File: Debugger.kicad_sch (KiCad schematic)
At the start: 24 parts, among them J1 Internal clock, J2 I/O, J3 NAND0, J4 NAND1, Q1 BC546, SW1 Single step, U1 NE555P, U2 74LS132, U3 74LS74

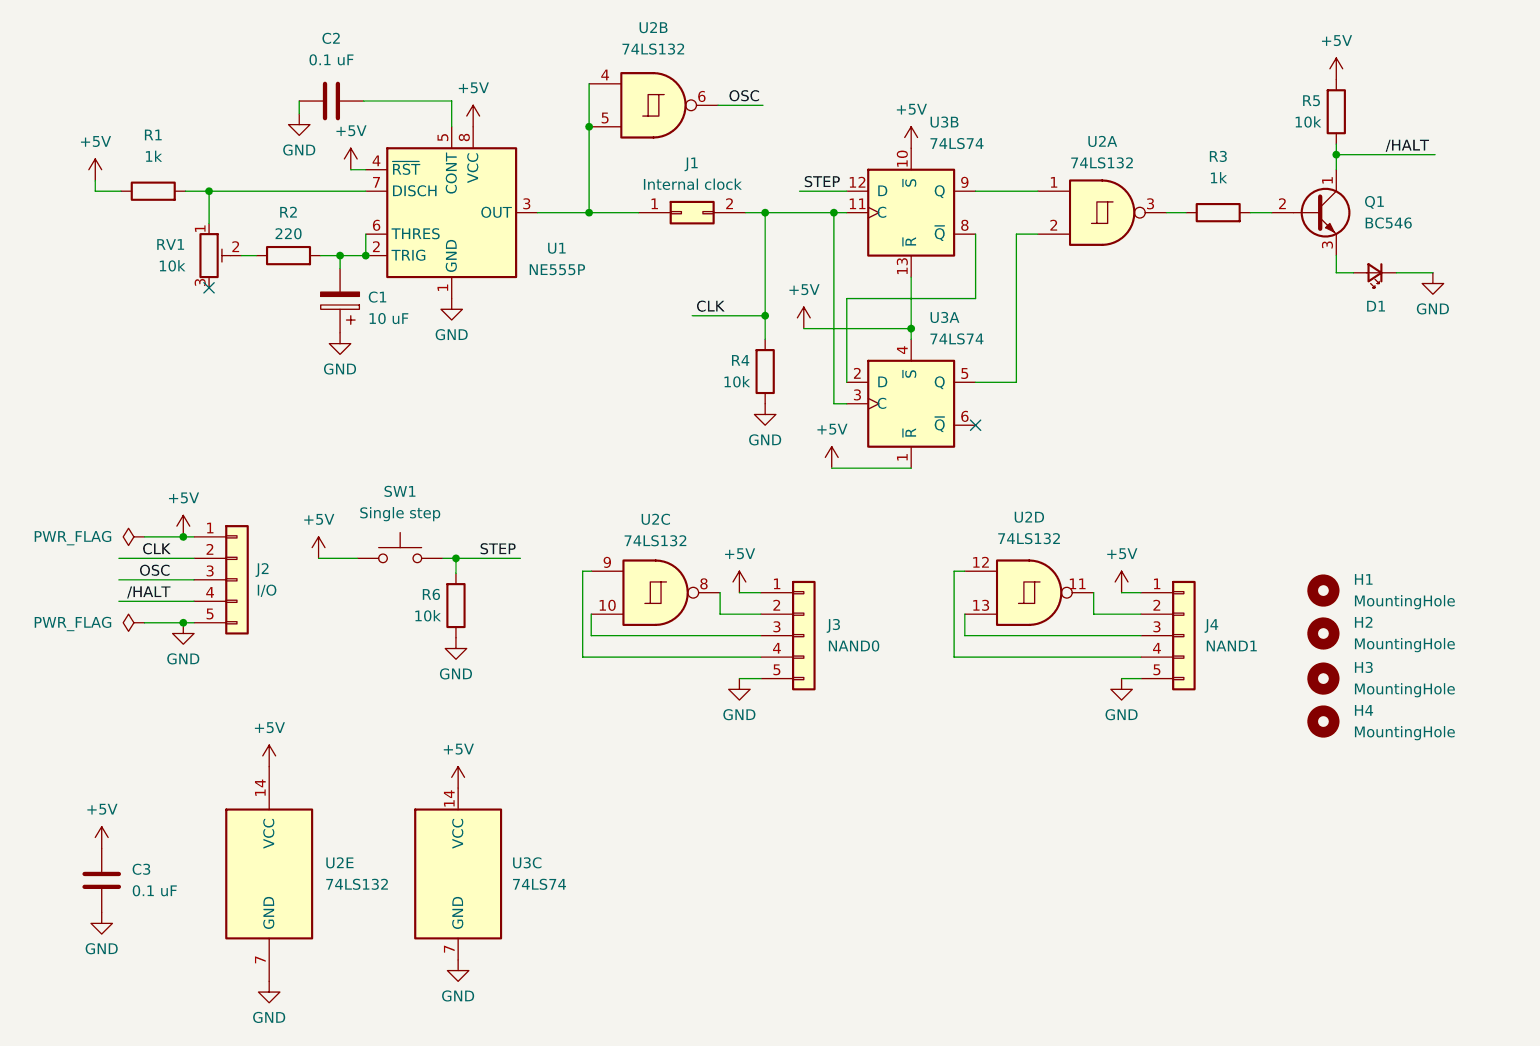
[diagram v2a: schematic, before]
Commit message: Board: add PCB drawing
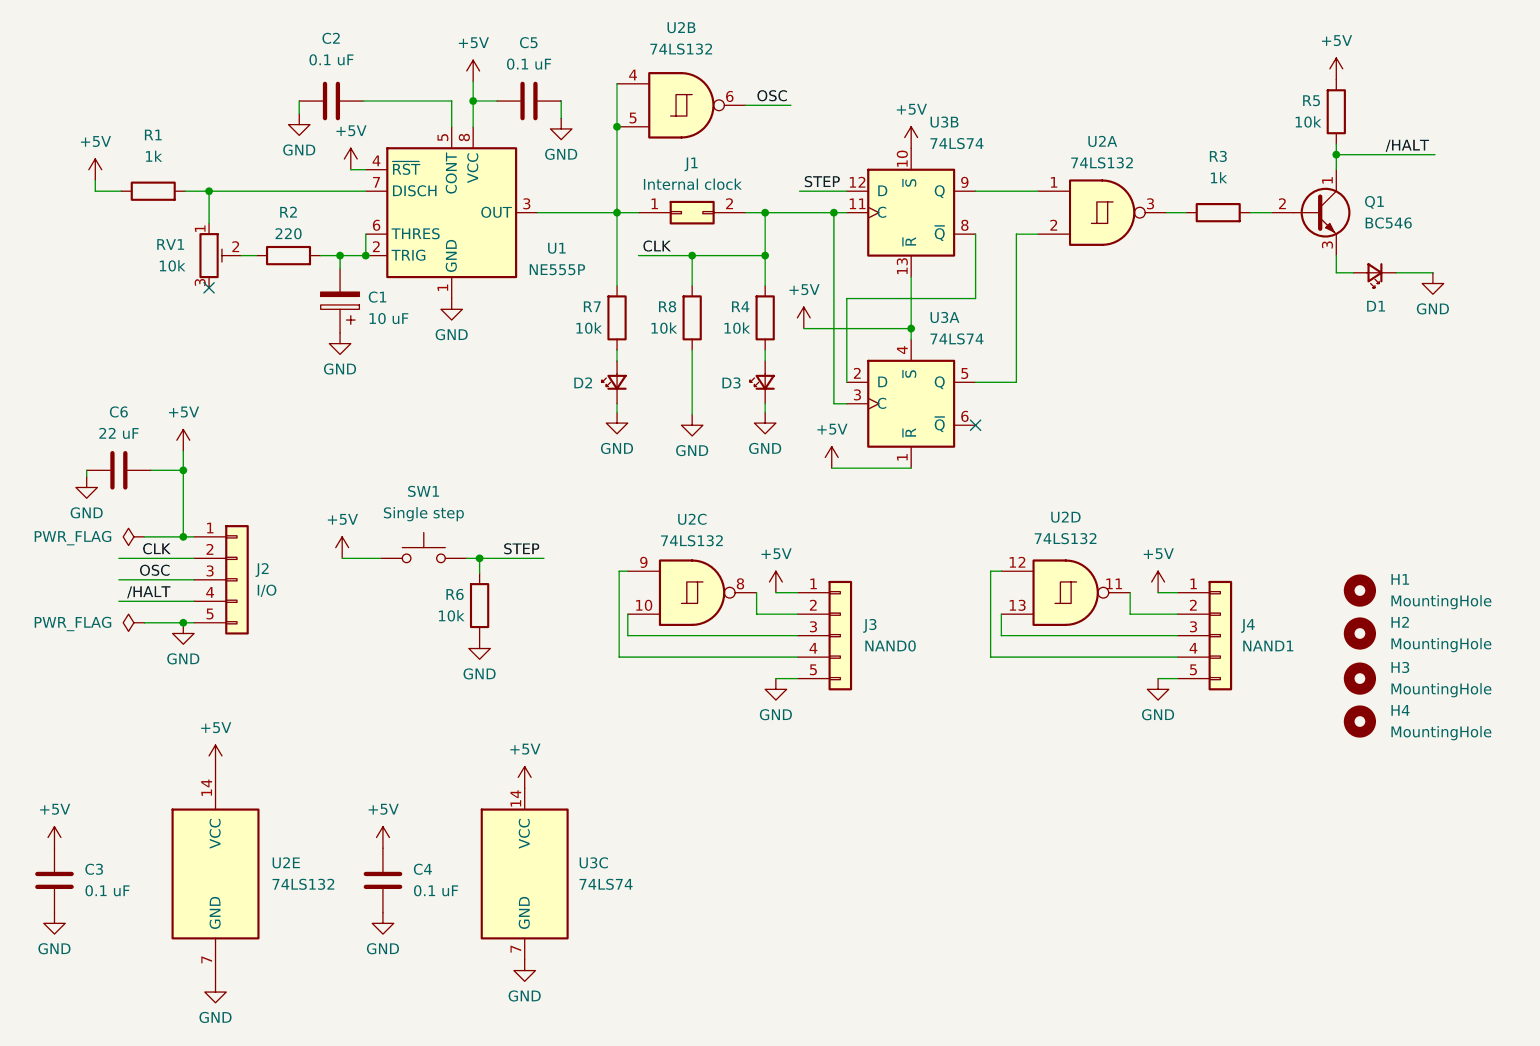
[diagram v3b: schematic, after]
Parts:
- added C4, C5: 0.1 uF, Capacitor_SMD:C_0603_1608Metric, symbol Device:C
- added C6: 22 uF, Capacitor_SMD:C_0603_1608Metric, symbol Device:C
- added D2, D3: LED_Small, LED_SMD:LED_0402_1005Metric, symbol Device:LED_Small
- added R7, R8: 10k, Resistor_SMD:R_0603_1608Metric, symbol Device:R
- C2, C3: footprint Capacitor_SMD:C_0201_0603Metric -> Capacitor_SMD:C_0603_1608Metric
- D1: footprint LED_SMD:LED_0201_0603Metric -> LED_SMD:LED_0402_1005Metric
- H1, H2, H3, H4: footprint MountingHole:MountingHole_2.2mm_M2 -> MountingHole:MountingHole_2.2mm_M2_DIN965_Pad
- J1: footprint Connector_PinHeader_1.00mm:PinHeader_2x01_P1.00mm_Vertical -> Connector_PinHeader_2.54mm:PinHeader_2x01_P2.54mm_Vertical
- J2, J3, J4: footprint Connector_PinHeader_1.00mm:PinHeader_1x05_P1.00mm_Vertical -> Connector_PinHeader_2.54mm:PinHeader_1x05_P2.54mm_Vertical
- R1, R2, R3, R4, R5, R6: footprint Resistor_SMD:R_0201_0603Metric -> Resistor_SMD:R_0603_1608Metric
- SW1: footprint Button_Switch_SMD:SW_Push_1P1T_NO_E-Switch_TL3301NxxxxxG -> Button_Switch_THT:SW_PUSH_6mm
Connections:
- net +5V: now also C4.2, C5.2, C6.1
- net CLK: now also R8.2
- net GND: now also C4.1, C5.1, C6.2, D2.1 (K), D3.1 (K), R8.1; no longer R4.1
- net at J1.1 (Pin_1), U1.3 (OUT), U2.4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: now also R7.2
- new net: D2.2 (A), R7.1
- new net: D3.2 (A), R4.1
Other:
- moved on the sheet: C3, H1, H2, H3, H4, J3, J4, R4, R6, SW1, U2B, U2C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

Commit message: Schematic, Board: fix D1 LED
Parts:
- added R9: 4.7k, Resistor_SMD:R_0603_1608Metric, symbol Device:R
- R4, R7: value 10k -> 4.7k
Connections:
- net +5V: now also R9.2
- net GND: now also Q1.3 (E); no longer D1.1 (K)
- net /HALT: now also D1.1 (K)
- net at D1.2 (A): now also R9.1; no longer Q1.3 (E)
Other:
- moved on the sheet: Q1, R3, R5, U2A

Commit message: Board: input header consistency
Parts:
- renumbered C2 to C1, C5 to C2, C1 to C3, C6 to C4, C3 to C5, C4 to C6, R5 to R2, R9 to R3, R2 to R4, R3 to R5, R8 to R6, R4 to R8, R6 to R9, U2 to U1, U1 to U2
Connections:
- net +5V: now also R1.2; no longer R1.1
- net CLK: now also J2.3 (Pin_3); no longer J2.2 (Pin_2)
- net OSC: now also J2.2 (Pin_2); no longer J2.3 (Pin_3)
- net at RV1.1, U2.7 (DISCH): now also R1.1; no longer R1.2
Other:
- moved on the sheet: C1, C2, C3, D2, D3, J1, R1, R4, R6, R7, R8, RV1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

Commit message: Board: revision 2
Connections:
- net CLK: now also J2.4 (Pin_4); no longer J2.3 (Pin_3)
- net GND: now also J2.2 (Pin_2), J3.2 (Pin_2), J4.2 (Pin_2); no longer J2.5 (Pin_5), J3.5 (Pin_5), J4.5 (Pin_5)
- net OSC: now also J2.3 (Pin_3); no longer J2.2 (Pin_2)
- net /HALT: now also J2.5 (Pin_5); no longer J2.4 (Pin_4)
- net at U1.8: now also J3.5 (Pin_5); no longer J3.2 (Pin_2)
- net at U1.11: now also J4.5 (Pin_5); no longer J4.2 (Pin_2)

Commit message: Board, Gerber: fail-safe pot resistor, production
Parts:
- added D4: LED Red, LED_SMD:LED_0603_1608Metric, symbol Device:LED_Small
- added R10: 1k, Resistor_SMD:R_0603_1608Metric, symbol Device:R
- added R4: 22k, Resistor_SMD:R_0603_1608Metric, symbol Device:R
- C4: footprint Capacitor_SMD:C_0603_1608Metric -> Capacitor_SMD:C_0805_2012Metric
- D1, D2, D3: value LED_Small -> LED Green; footprint LED_SMD:LED_0402_1005Metric -> LED_SMD:LED_0603_1608Metric
- J1: value Internal clock -> male
- J2: value I/O -> male
- J3: value NAND0 -> male
- J4: value NAND1 -> male
- R3: value 4.7k -> 1k
- R5: renamed from R4; value 220 -> 220R
- R8: renamed from R7; value 4.7k -> 1k
- R9: renamed from R8; value 4.7k -> 1k
- SW1: value Single step -> push button
- renumbered R9 to R11, R5 to R6, R6 to R7
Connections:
- net +5V: now also R10.2
- net GND: now also D4.1 (K)
- net at C3.2, R5.2, U2.2 (TRIG)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: now also R4.1
- net at R1.1, RV1.1, U2.7 (DISCH): now also R4.2
- new net: D4.2 (A), R10.1
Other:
- note added: "Internal oscillator"
- note added: "Single step"
- moved on the sheet: C3, C4, R1, R11, R5, RV1, SW1
